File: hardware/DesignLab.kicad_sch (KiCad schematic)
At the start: 88 parts, among them J1 Micro_SD_Card_Det, J2 Conn_01x04_Female, P1 USB_C_Plug_USB2.0, Q1 DMG3415U-7, SW1 SW_DPDT_x2, SW10 Button, SW11 Button, SW12 RESET, SW13 ON, SW14 VOL, SW15 BOOT, SW2 SW_DPDT_x2, SW3 REC, SW4 Button, SW5 Button, SW6 Button, SW7 Button, SW8 Button, SW9 Button, U1 SPH0641LM4H, U10 MCP4018-xxxxLT, U2 RP2040, U3 QRE1113, U4 QRE1113, U5 QRE1113, U6 AT25SF128A, U7 PAM8302AAD, U8 AP2112K-3.3, U9 QRE1113, Y1 12Mhz

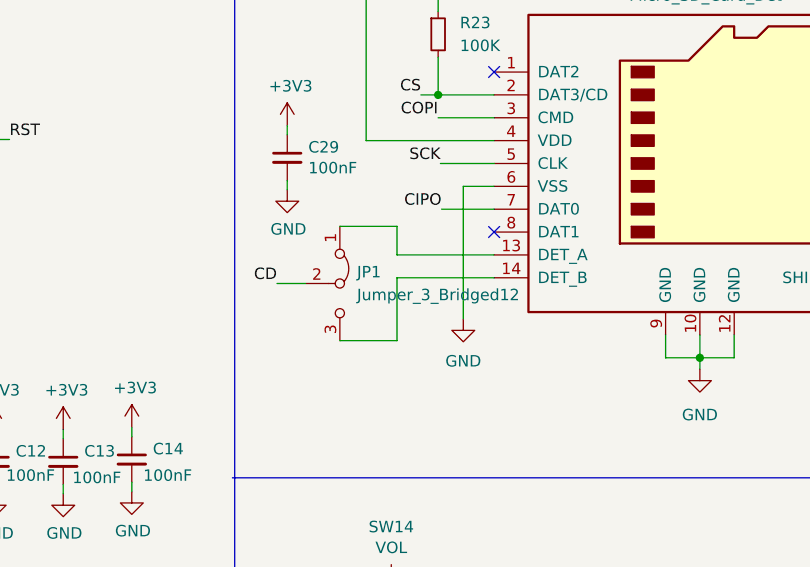
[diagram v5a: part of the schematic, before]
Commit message: 3D model assigned
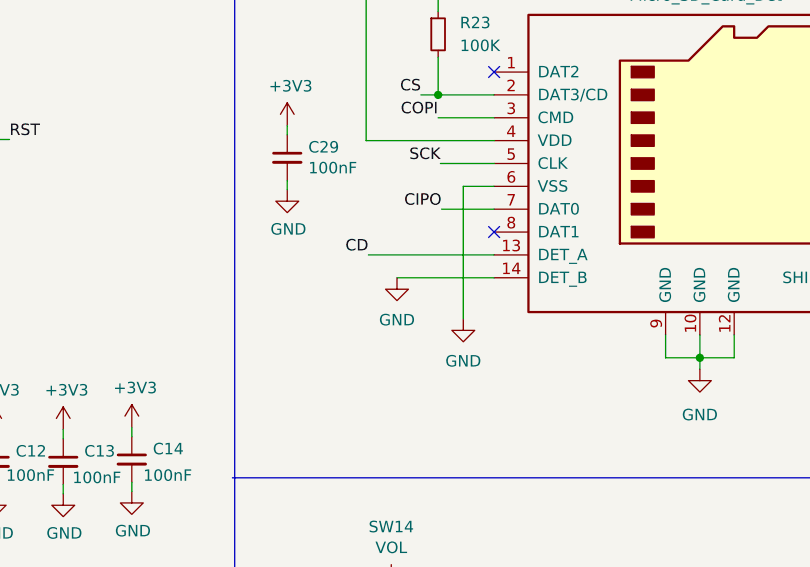
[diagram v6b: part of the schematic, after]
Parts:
- removed JP1: Jumper_3_Bridged12, Jumper:SolderJumper-3_P1.3mm_Bridged12_RoundedPad1.0x1.5mm, symbol Jumper:Jumper_3_Bridged12
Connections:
- net CD: now also J1.13 (DET_A)
- net GND: now also J1.14 (DET_B)
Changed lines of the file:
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@@
     (stroke (width 0) (type default) (color 0 0 0 0))
   )
-  (wire (pts (xy 215.265 53.34) (xy 221.615 53.34))
-    (stroke (width 0) (type default) (color 0 0 0 0))
-  )
   (wire (pts (xy 111.379 40.513) (xy 112.776 40.513))
     (stroke (width 0) (type default) (color 0 0 0 0))
@@
     (stroke (width 0) (type default) (color 0 0 0 0))
   )
-  (wire (pts (xy 221.615 56.515) (xy 232.41 56.515))
-    (stroke (width 0) (type default) (color 0 0 0 0))
-  )
   (wire (pts (xy 279.146 173.736) (xy 279.146 178.562))
     (stroke (width 0) (type default) (color 0 0 0 0))
@@
     (stroke (width 0) (type default) (color 0 0 0 0))
   )
-  (wire (pts (xy 221.615 66.04) (xy 221.615 59.055))
-    (stroke (width 0) (type default) (color 0 0 0 0))
-  )
   (wire (pts (xy 87.63 186.69) (xy 87.63 185.42))
     (stroke (width 0) (type default) (color 0 0 0 0))
@@
     (stroke (width 0) (type default) (color 0 0 0 0))
   )
-  (wire (pts (xy 215.265 66.04) (xy 221.615 66.04))
-    (stroke (width 0) (type default) (color 0 0 0 0))
-  )
   (wire (pts (xy 172.72 104.394) (xy 172.72 103.378))
     (stroke (width 0) (type default) (color 0 0 0 0))
@@
     (stroke (width 0) (type default) (color 0 0 0 0))
   )
-  (wire (pts (xy 208.28 59.69) (xy 211.455 59.69))
+  (wire (pts (xy 218.44 56.515) (xy 232.41 56.515))
     (stroke (width 0) (type default) (color 0 0 0 0))
   )
@@
     (stroke (width 0) (type default) (color 0 0 0 0))
   )
-  (wire (pts (xy 221.615 53.34) (xy 221.615 56.515))
-    (stroke (width 0) (type default) (color 0 0 0 0))
-  )
   (wire (pts (xy 146.685 227.965) (xy 146.685 229.87))
     (stroke (width 0) (type default) (color 0 0 0 0))
@@
     (effects (font (size 1.27 1.27)) (justify right bottom))
   )
-  (label "CD" (at 208.28 59.69 180)
+  (label "CD" (at 218.44 56.515 180)
     (effects (font (size 1.27 1.27)) (justify right bottom))
   )
@@
     (pin "1")
   )
-  (symbol (lib_id "Jumper:Jumper_3_Bridged12") (at 215.265 59.69 270) (unit 1)
-    (in_bom yes) (on_board yes) (fields_autoplaced)
-    (property "Reference" "JP1" (id 0) (at 217.17 58.4199 90)
-      (effects (font (size 1.27 1.27)) (justify left))
-    )
-    (property "Value" "Jumper_3_Bridged12" (id 1) (at 217.17 60.9599 90)
-      (effects (font (size 1.27 1.27)) (justify left))
-    )
-    (property "Footprint" "Jumper:SolderJumper-3_P1.3mm_Bridged12_RoundedPad1.0x1.5mm" (id 2) (at 215.265 59.69 0)
-      (effects (font (size 1.27 1.27)) hide)
-    )
-    (property "Datasheet" "~" (id 3) (at 215.265 59.69 0)
-      (effects (font (size 1.27 1.27)) hide)
-    )
-    (pin "1")
-    (pin "2")
-    (pin "3")
-  )
   (symbol (lib_id "power:GND") (at 212.725 149.225 180) (unit 1)
     (in_bom yes) (on_board yes)
@@
     (pin "1")
   )
+  (symbol (lib_name "GND_1") (lib_id "power:GND") (at 221.615 59.055 0) (unit 1)
+    (in_bom yes) (on_board yes) (fields_autoplaced)
+    (property "Reference" "#PWR?" (id 0) (at 221.615 65.405 0)
+      (effects (font (size 1.27 1.27)) hide)
+    )
+    (property "Value" "GND" (id 1) (at 221.615 63.754 0))
+    (property "Footprint" "" (id 2) (at 221.615 59.055 0)
+      (effects (font (size 1.27 1.27)) hide)
+    )
+    (property "Datasheet" "" (id 3) (at 221.615 59.055 0)
+      (effects (font (size 1.27 1.27)) hide)
+    )
+    (pin "1")
+  )
   (symbol (lib_id "Device:R_Small") (at 227.076 109.855 270) (unit 1)
     (in_bom yes) (on_board yes)
@@
       (reference "#PWR0130") (unit 1) (value "GND") (footprint "")
     )
+    (path "/4cede614-f863-434b-a614-82cce2d82a79"
+      (reference "#PWR?") (unit 1) (value "GND") (footprint "")
+    )
     (path "/b787c517-ecac-40e0-a211-870160b2f519"
       (reference "BT4") (unit 1) (value "Battery_Cell") (footprint "Connector_PinHeader_2.54mm:PinHeader_1x02_P2.54mm_Vertical")
@@
       (reference "J2") (unit 1) (value "Conn_01x04_Female") (footprint "Connector_PinHeader_2.54mm:PinHeader_1x04_P2.54mm_Vertical")
     )
-    (path "/20818890-3d12-4931-9b0f-a230e9d9d177"
-      (reference "JP1") (unit 1) (value "Jumper_3_Bridged12") (footprint "Jumper:SolderJumper-3_P1.3mm_Bridged12_RoundedPad1.0x1.5mm")
-    )
     (path "/0573c5a0-e569-4ade-86fb-e7b4b3dd072d"

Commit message: Corrections to the schematic and the PCB
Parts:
- BT4: value Battery_Cell -> (none); footprint Connector_PinHeader_2.54mm:PinHeader_1x02_P2.54mm_Vertical -> (none)
- BZ1: value Buzzer -> (none); footprint Connector_PinHeader_2.54mm:PinHeader_1x02_P2.54mm_Vertical -> (none)
- C1, C3: value 27pF -> (none); footprint Capacitor_SMD:C_0603_1608Metric -> (none)
- C10, C11, C12, C13, C14, C15, C16, C5, C6, C8, C9: value 100nF -> (none); footprint Capacitor_SMD:C_0402_1005Metric_Pad0.74x0.62mm_HandSolder -> (none)
- C17, C18, C19, C28: value 10nF -> (none); footprint Capacitor_SMD:C_0603_1608Metric -> (none)
- C2: value 0.1uF -> (none); footprint Capacitor_SMD:C_0402_1005Metric_Pad0.74x0.62mm_HandSolder -> (none)
- C20: value 47uF -> (none); footprint Capacitor_SMD:C_0603_1608Metric -> (none)
- C21, C22, C4, C7: value 1uF -> (none); footprint Capacitor_SMD:C_0603_1608Metric -> (none)
- C23, C24: value 220pF -> (none); footprint Capacitor_SMD:C_0603_1608Metric -> (none)
- C25, C26, C27: value 10uF -> (none); footprint Capacitor_SMD:C_0402_1005Metric_Pad0.74x0.62mm_HandSolder -> (none)
- C29: value 100nF -> (none); footprint Capacitor_SMD:C_0402_1005Metric -> (none)
- D1: value MBR120 -> (none); footprint Design:SODFL3616X98N -> (none)
- D2: value LED -> (none); footprint Capacitor_SMD:C_0603_1608Metric -> (none)
- F1: value 0.5A -> (none); footprint Fuse:Fuse_0805_2012Metric -> (none)
- J1: value Micro_SD_Card_Det -> (none); footprint Design:1140084168 -> (none)
- J2: value Conn_01x04_Female -> (none); footprint Connector_PinHeader_2.54mm:PinHeader_1x04_P2.54mm_Vertical -> (none)
- P1: value USB_C_Plug_USB2.0 -> (none); footprint Connectors:C393939 -> (none)
- Q1: value DMG3415U-7 -> (none); footprint Package_TO_SOT_SMD:SOT-23 -> (none)
- R1: value 1K -> (none); footprint Resistor_SMD:R_0603_1608Metric -> (none)
- R10, R11, R12, R22: value 220 -> (none); footprint Capacitor_SMD:C_0603_1608Metric -> (none)
- R13: value 1.8K -> (none); footprint Resistor_SMD:R_0603_1608Metric -> (none)
- R14, R15, R9: value 100 -> (none); footprint Resistor_SMD:R_0603_1608Metric -> (none)
- R16: value 10K -> (none); footprint Resistor_SMD:R_0603_1608Metric -> (none)
- R17, R23: value 100K -> (none); footprint Resistor_SMD:R_0603_1608Metric -> (none)
- R18, R19: value 5k1 -> (none); footprint Resistor_SMD:R_0603_1608Metric -> (none)
- R2, R3: value 27 -> (none); footprint Resistor_SMD:R_0603_1608Metric -> (none)
- R20: value 330 -> (none); footprint Resistor_SMD:R_0603_1608Metric -> (none)
- R21, R4, R6, R7: value 100 -> (none); footprint Capacitor_SMD:C_0603_1608Metric -> (none)
- R5: value 4K7 -> (none); footprint Resistor_SMD:R_0603_1608Metric -> (none)
- R8: value 220 -> (none); footprint Resistor_SMD:R_0603_1608Metric -> (none)
- SW1: value SW_DPDT_x2 -> (none); footprint Design:OS102011MA1QN1 -> (none)
- SW10, SW11, SW4, SW5, SW6, SW7, SW8, SW9: value Button -> (none); footprint Design:EVQPLFA08 -> (none)
- SW12: value RESET -> (none); footprint Button_Switch_SMD:SW_SPST_TL3342 -> (none)
- SW13: value ON -> (none); footprint Design:OS102011MA1QN1 -> (none)
- SW14: value VOL -> (none); footprint Button_Switch_SMD:SW_SPST_TL3342 -> (none)
- SW15: value BOOT -> (none); footprint Button_Switch_SMD:SW_SPST_TL3342 -> (none)
- SW3: value REC -> (none); footprint Button_Switch_SMD:SW_SPST_TL3342 -> (none)
- U1: value SPH0641LM4H -> (none); footprint Sensors:MIC_SPH0641LM4H-1 -> (none)
- U10: value MCP4018-xxxxLT -> (none); footprint Design:SOT65P210X110-6N -> (none)
- U2: value RP2040 -> (none); footprint badge_pwnCon:RP2040-QFN-56 -> (none)
- U3, U4, U5, U9: value QRE1113 -> (none); footprint Design:QRE1113 -> (none)
- U6: value AT25SF128A -> (none); footprint Design:SOIC127P798X216-8N -> (none)
- U7: value PAM8302AAD -> (none); footprint Package_SO:MSOP-8_3x3mm_P0.65mm -> (none); LCSC# C112137 -> (none); Stock en EC Yes -> No; manf# PAM8302AADCR -> PAM8302AASCR; provedor LCSC -> MOUSER
- U8: value AP2112K-3.3 -> (none); footprint Package_TO_SOT_SMD:SOT-23-5 -> (none)
- Y1: value 12Mhz -> (none); footprint Crystal:Crystal_SMD_HC49-SD -> (none)
- sw2: renamed from SW2; value SW_DPDT_x2 -> (none); footprint Design:OS102011MA1QN1 -> (none); manf# OS102011MS2QN1 -> 7829H-1-023LF
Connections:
- net SCL: now also U10.3 (SCL); no longer U10.4 (SDA)
- net SDA: now also U10.4 (SDA); no longer U10.3 (SCL)
